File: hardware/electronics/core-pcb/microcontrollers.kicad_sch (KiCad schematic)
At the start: 34 parts, among them IC7 ATSAME53J18A-MF, U6 ATSAMD11D14A-M

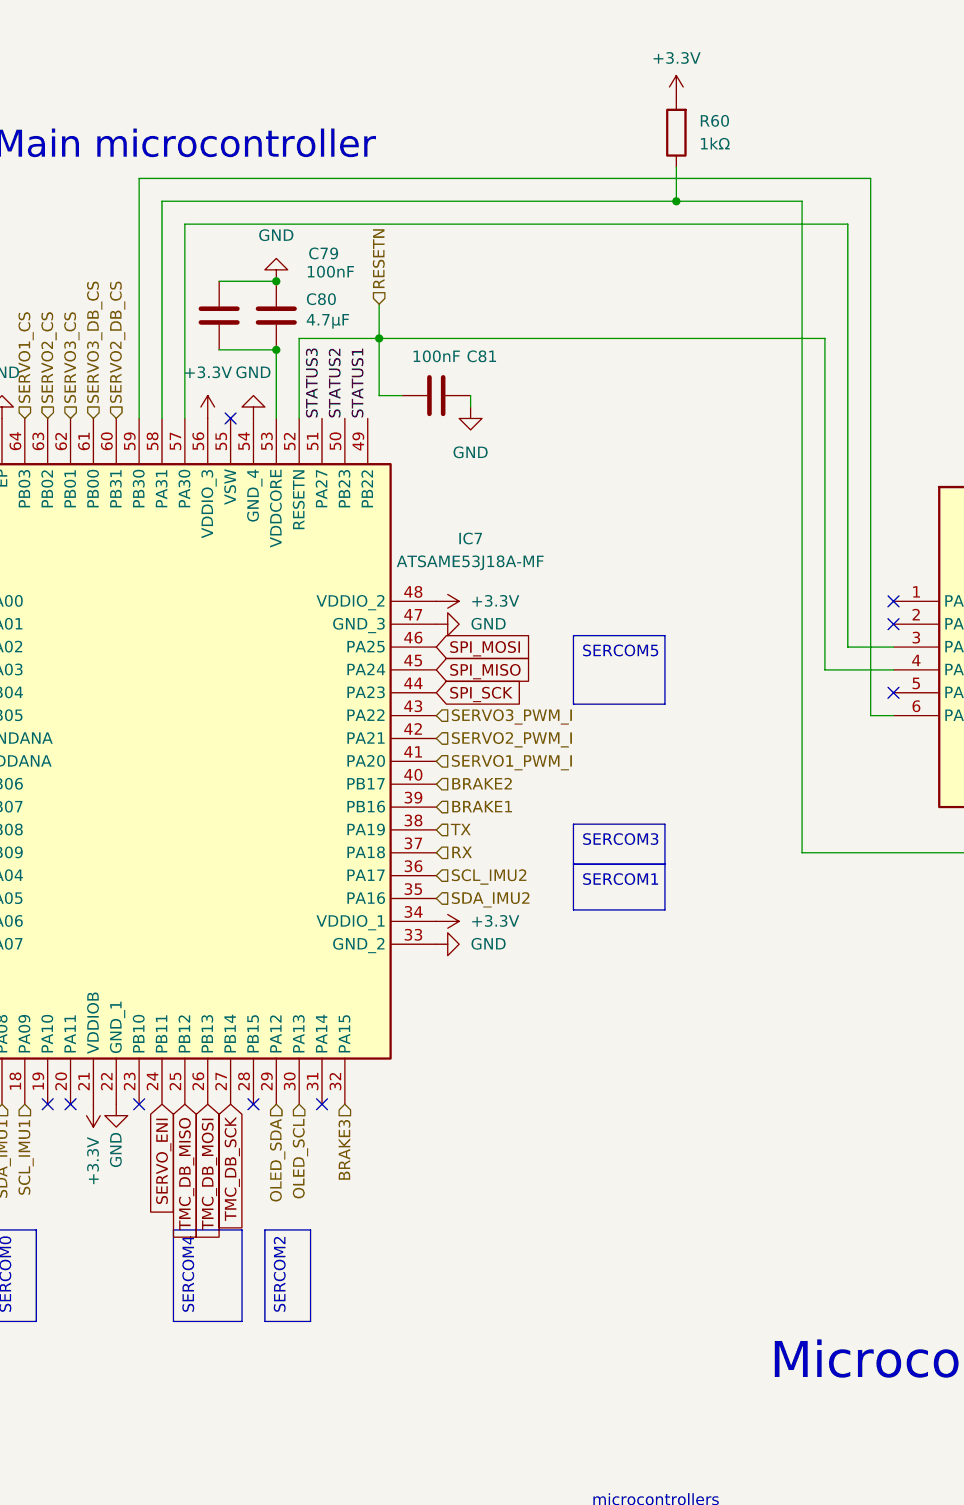
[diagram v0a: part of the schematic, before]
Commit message: removed pullup resistor on swdio as it is too small
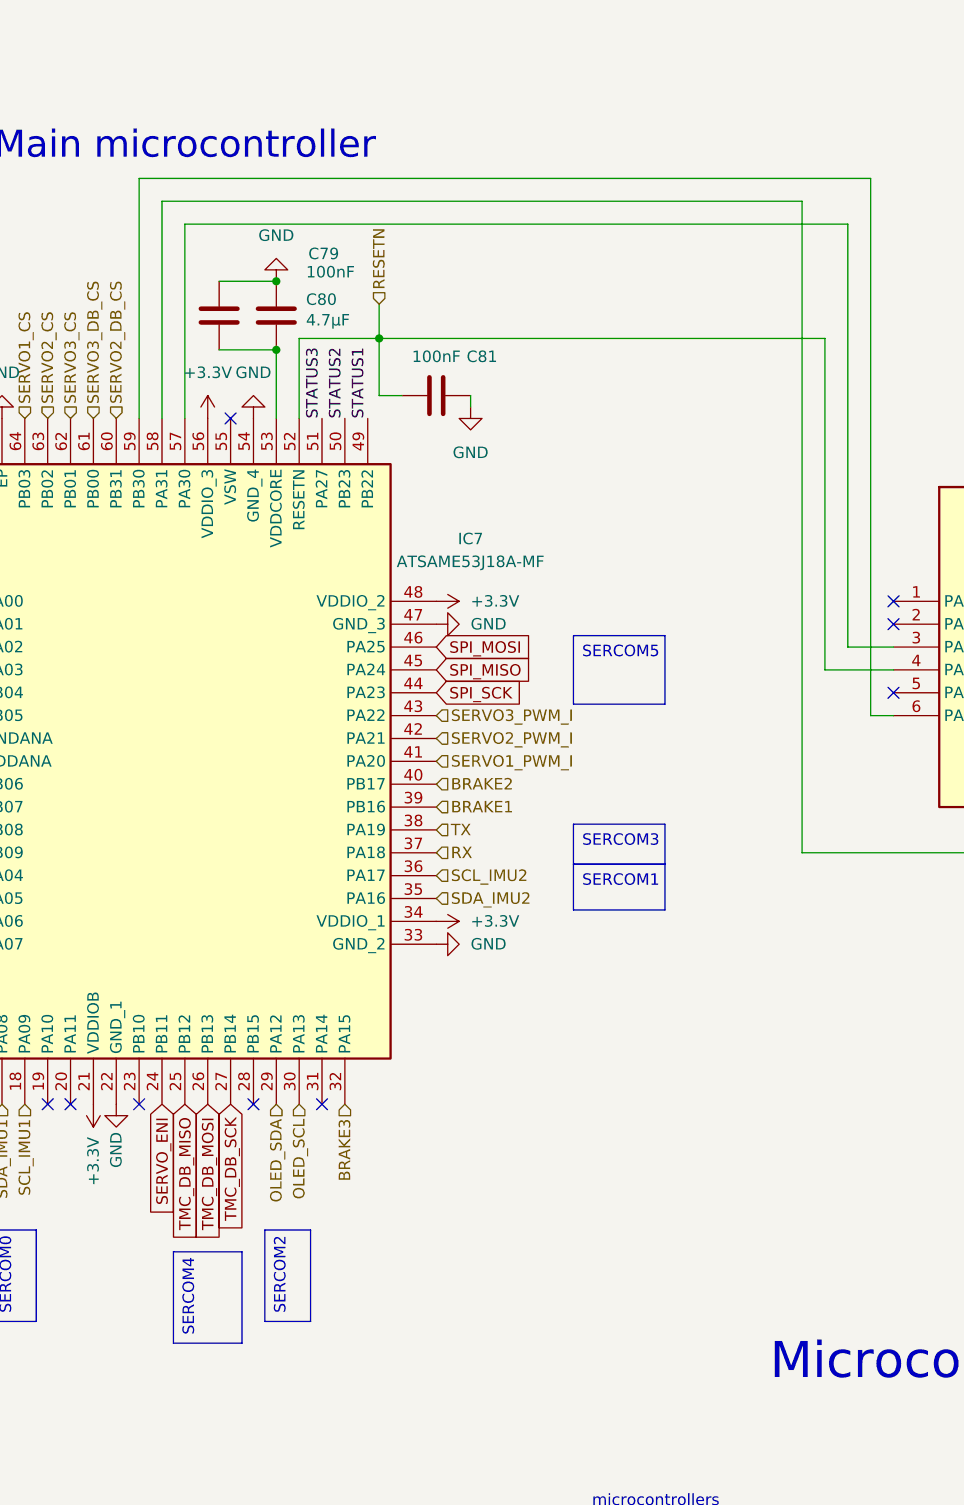
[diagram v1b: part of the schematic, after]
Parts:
- removed R60: 1kΩ, Resistor_SMD:R_0603_1608Metric, symbol Device:R
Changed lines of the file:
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@@
 	(text_box "SERCOM4"
 		(exclude_from_sim no)
-		(at 144.78 160.02 90)
+		(at 144.78 162.44 90)
 		(size 7.62 10.16)
 		(margins 0.9525 0.9525 0.9525 0.9525)
@@
 	)
 	(junction
-		(at 200.66 45.72)
-		(diameter 0)
-		(color 0 0 0 0)
-	)
-	(junction
 		(at 35.56 66.04)
 		(diameter 0)
@@
 	(wire
 		(pts
-			(xy 200.66 45.72) (xy 214.63 45.72)
-		)
-		(stroke
-			(width 0)
-			(type default)
-		)
-	)
-	(wire
-		(pts
 			(xy 265.43 90.17) (xy 267.97 90.17)
 		)
@@
 	(wire
 		(pts
-			(xy 200.66 41.91) (xy 200.66 45.72)
-		)
-		(stroke
-			(width 0)
-			(type default)
-		)
-	)
-	(wire
-		(pts
 			(xy 74.93 33.02) (xy 85.09 33.02)
 		)
@@
 	(wire
 		(pts
-			(xy 143.51 45.72) (xy 200.66 45.72)
+			(xy 143.51 45.72) (xy 214.63 45.72)
 		)
 		(stroke
@@
 	)
 	(symbol
-		(lib_id "power:+3.3V")
-		(at 200.66 34.29 0)
-		(unit 1)
-		(exclude_from_sim no)
-		(in_bom yes)
-		(on_board yes)
-		(dnp no)
-		(fields_autoplaced yes)
-		(property "Reference" "#PWR0157"
-			(at 200.66 38.1 0)
-			(effects
-				(font
-					(size 1.27 1.27)
-				)
-				(hide yes)
-			)
-		)
-		(property "Value" "+3.3V"
-			(at 200.66 29.845 0)
-			(effects
-				(font
-					(size 1.27 1.27)
-				)
-			)
-		)
-		(property "Footprint" ""
-			(at 200.66 34.29 0)
-			(effects
-				(font
-					(size 1.27 1.27)
-				)
-				(hide yes)
-			)
-		)
-		(property "Datasheet" ""
-			(at 200.66 34.29 0)
-			(effects
-				(font
-					(size 1.27 1.27)
-				)
-				(hide yes)
-			)
-		)
-		(property "Description" "Power symbol creates a global label with name \"+3.3V\""
-			(at 200.66 34.29 0)
-			(effects
-				(font
-					(size 1.27 1.27)
-				)
-				(hide yes)
-			)
-		)
-		(pin "1"
-		)
-		(instances
-			(project "motordriver"
-				(path "/c7634e88-16d1-45ec-9aac-9c841e03cf6d/9ebbb593-eaf1-4a56-ba2a-164e20b1d55e"
-					(reference "#PWR0157")
-					(unit 1)
-				)
-			)
-		)
-	)
-	(symbol
 		(lib_id "Device:R")
 		(at 54.61 119.38 180)
@@
 					(unit 1)
 				)
-			)
-		)
-	)
-	(symbol
-		(lib_id "Device:R")
-		(at 200.66 38.1 180)
-		(unit 1)
-		(exclude_from_sim no)
-		(in_bom yes)
-		(on_board yes)
-		(dnp no)
-		(fields_autoplaced yes)
-		(property "Reference" "R60"
-			(at 203.2 36.8299 0)
-			(effects
-				(font
-					(size 1.27 1.27)
-				)
-				(justify right)
-			)
-		)
-		(property "Value" "1kΩ"
-			(at 203.2 39.3699 0)
-			(effects
-				(font
-					(size 1.27 1.27)
-				)
-				(justify right)
-			)
-		)
-		(property "Footprint" "Resistor_SMD:R_0603_1608Metric"
-			(at 202.438 38.1 90)
-			(effects
-				(font
-					(size 1.27 1.27)
-				)
-				(hide yes)
-			)
-		)
-		(property "Datasheet" "~"
-			(at 200.66 38.1 0)
-			(effects
-				(font
-					(size 1.27 1.27)
-				)
-				(hide yes)
-			)
-		)
-		(property "Description" "Resistor"
-			(at 200.66 38.1 0)
-			(effects
-				(font
-					(size 1.27 1.27)
-				)
-				(hide yes)
-			)
-		)
-		(pin "1"
-		)
-		(pin "2"
-		)
-		(instances
-			(project "motordriver"
-				(path "/c7634e88-16d1-45ec-9aac-9c841e03cf6d/9ebbb593-eaf1-4a56-ba2a-164e20b1d55e"
-					(reference "R60")
-					(unit 1)
-				)

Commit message: started work on pcbv2 work in progress
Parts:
- renumbered C67 to C58, C68 to C59, C69 to C60, C70 to C61, C71 to C62, C72 to C63, C73 to C64, C74 to C65, C75 to C66, C76 to C67, C77 to C68, C78 to C69, C79 to C70, C80 to C71, C81 to C72, C82 to C73, D29 to D26, D30 to D27, D31 to D28, D32 to D29, D33 to D30, D34 to D31, D35 to D32, IC7 to IC6, R55 to R44, R56 to R45, R57 to R46, R58 to R47, R59 to R48, R61 to R49, R62 to R50, R63 to R51, U6 to U5
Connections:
- net CLK: now reaches IC6.57 (PA30)
- net CLK: now also U5.7 (PA08); no longer U5.3 (PA04)
- net SWO: now reaches IC6.59 (PB30), U5.6 (PA07)
- net DIO: now reaches IC6.58 (PA31)
- net DIO: now also U5.3 (PA04); no longer U5.7 (PA08)
